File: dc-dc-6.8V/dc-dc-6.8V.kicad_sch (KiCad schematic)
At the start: 23 parts, among them P1 1.8mm_16AWG, P2 1.8mm_16AWG, P3 1.8mm_16AWG, P4 1.8mm_16AWG, Q3 DOD4185, U2 LM25085MY/NOPB

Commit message: update
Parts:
- removed C10: 1nF, bio-robot:C_0603_1608Metric, symbol bio-robot:C_1nF
- removed C11: 3.3nF, bio-robot:C_0603_1608Metric, symbol bio-robot:C_3.3nF
- removed C12: 47uF, bio-robot:CAP_EEEFT1H470AP, symbol bio-robot:Cpol_EEEFT1H470AP
- removed C9: 0.47u, bio-robot:C_0603_1608Metric, symbol bio-robot:C_0.47u
- removed D2: STPS20M100SG-TR, bio-robot:TO-263-2, symbol bio-robot:D_STPS20M100SG-TR
- removed L2: 3.3uH, bio-robot:IND_MDA1050-3R3M, symbol bio-robot:L_MDA1050-3R3M
- removed Q3: DOD4185, bio-robot:DPAK-3_ONS, symbol bio-robot:Q_Pch40V45A
- removed R3: 113k, bio-robot:R_0603_1608Metric, symbol bio-robot:R_113k
- removed R4: 4.12k, bio-robot:R_0603_1608Metric, symbol bio-robot:R_4.12k
- removed R5: 10m, bio-robot:R_0805_2012Metric, symbol bio-robot:R_10m_0805
- removed R8: 10k, bio-robot:R_0603_1608Metric, symbol bio-robot:R_10k
- removed R9: 2.26k, bio-robot:R_0603_1608Metric, symbol bio-robot:R_2.26k
- removed U2: LM25085MY/NOPB, bio-robot:MSOP8_PowerPad, symbol bio-robot:LM25085MY_NOPB
- added C3: 22u_1206, bots:C_1206_3216Metric, symbol bots:C_22u_1206
- added C4: 0.1u, bots:C_0603_1608Metric, symbol bots:C_0.1u
- added C5: 15nF, bio-robot:C_0603_1608Metric, symbol bio-robot:C_15nF
- added C6: 0.47u, bio-robot:C_0603_1608Metric, symbol bio-robot:C_0.47u
- added C7: 2.2u, bio-robot:C_0603_1608Metric, symbol bio-robot:C_2.2u
- added C8: 180pF, bio-robot:C_0603_1608Metric, symbol bio-robot:C_180pF
- added C9: 82uF, bio-robot:CAP_10SVPC120MV, symbol bio-robot:Cpol_82uF
- added L1: 1.8uH, bio-robot:IND_XAL7070_COC, symbol bio-robot:L_XAL7070-182MEC
- added Q1, Q2: SVD5865NLT4G, bots:DPAK-3_ONS, symbol bio-robot:Q_Nch60V46A
- added R1: 137k, bio-robot:R_0603_1608Metric, symbol bio-robot:R_137k
- added R2: 806R, bots:R_0603_1608Metric, symbol bio-robot:R_806R
- added R3: 9.76k, bots:R_0603_1608Metric, symbol bio-robot:R_9.76k
- added R4: 102k, bots:R_0603_1608Metric, symbol bio-robot:R_102k
- added U1: LM3150MHX_NOPB, bio-robot:SOP65P640X110-15N, symbol bio-robot:LM3150MHX_NOPB
- H1: renamed from H5; footprint MountingHole:MountingHole_3.2mm_M3_DIN965_Pad -> bio-robot:MountingHole_3.2mm_M3_DIN965_Pad
- H2: renamed from H6; footprint MountingHole:MountingHole_3.2mm_M3_DIN965_Pad -> bio-robot:MountingHole_3.2mm_M3_DIN965_Pad
- H3: renamed from H7; footprint MountingHole:MountingHole_3.2mm_M3_DIN965_Pad -> bio-robot:MountingHole_3.2mm_M3_DIN965_Pad
- H4: renamed from H8; footprint MountingHole:MountingHole_3.2mm_M3_DIN965_Pad -> bio-robot:MountingHole_3.2mm_M3_DIN965_Pad
- renumbered C8 to C1, C7 to C2
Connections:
- net +6.8V: now also C8.1, C9.1, L1.1, R4.1
- net CVCC: now also C7.1, U1.1 (VCC)
- net GND: now also C3.2, C4.2, C5.2, C7.2, C9.2, Q2.3 (S), R3.2, U1.14 (PGND), U1.15 (EXP), U1.5 (SGND_5), U1.9 (SGND_9)
- net VCC: now also C3.1, C4.1, Q1.2 (D), R1.1, U1.2 (VIN)
- new net BST: C6.1, U1.12 (BST)
- new net FB: C8.2, R3.1, R4.2, U1.4 (FB)
- new net HG: Q1.1 (G), U1.11 (HG)
- new net ILIM: R2.1, U1.8 (ILIM)
- new net LG: Q2.1 (G), U1.13 (LG)
- new net RON: R1.2, U1.7 (RON)
- new net SS: C5.1, U1.6 (SS)
- new net SW: C6.2, L1.2, Q1.3 (S), Q2.2 (D), R2.2, U1.10 (SW)
- no-connect marks 0 -> 1
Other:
- moved on the sheet: C1, C2, H1, H2, H3, H4, P1, P2, P3, P4

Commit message: update
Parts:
- removed Q1, Q2: SVD5865NLT4G, bots:DPAK-3_ONS, symbol bio-robot:Q_Nch60V46A
- added Q1, Q2: SVD5865NLT4G, bio-robot:SOIC-8_3.9x4.9mm_P1.27mm, symbol bio-robot:Q_Nch60V46A_SOIC8
- C1, C2, C3: footprint bots:C_1206_3216Metric -> bio-robot:C_1206_3216Metric; symbol bots:C_22u_1206 -> bio-robot:C_22u_1206
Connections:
- net GND: now also Q2.1 (S), Q2.2 (S), Q2.3 (S)
- net HG: now also Q1.4 (G)
- net LG: now also Q2.4 (G)
- net SW: now also Q1.1 (S), Q1.2 (S), Q1.3 (S), Q2.5 (D), Q2.6 (D), Q2.7 (D), Q2.8 (D)
- net VCC: now also Q1.5 (D), Q1.6 (D), Q1.7 (D), Q1.8 (D)

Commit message: update to silkscreen
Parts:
- Q1, Q2: value SVD5865NLT4G -> AO4354
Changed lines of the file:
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@@
 			)
 		)
-		(property "Value" "SVD5865NLT4G"
+		(property "Value" "AO4354"
 			(at 179.07 100.9649 0)
 			(show_name no)
@@
 			)
 		)
-		(property "Value" "SVD5865NLT4G"
+		(property "Value" "AO4354"
 			(at 179.07 67.9449 0)
 			(show_name no)

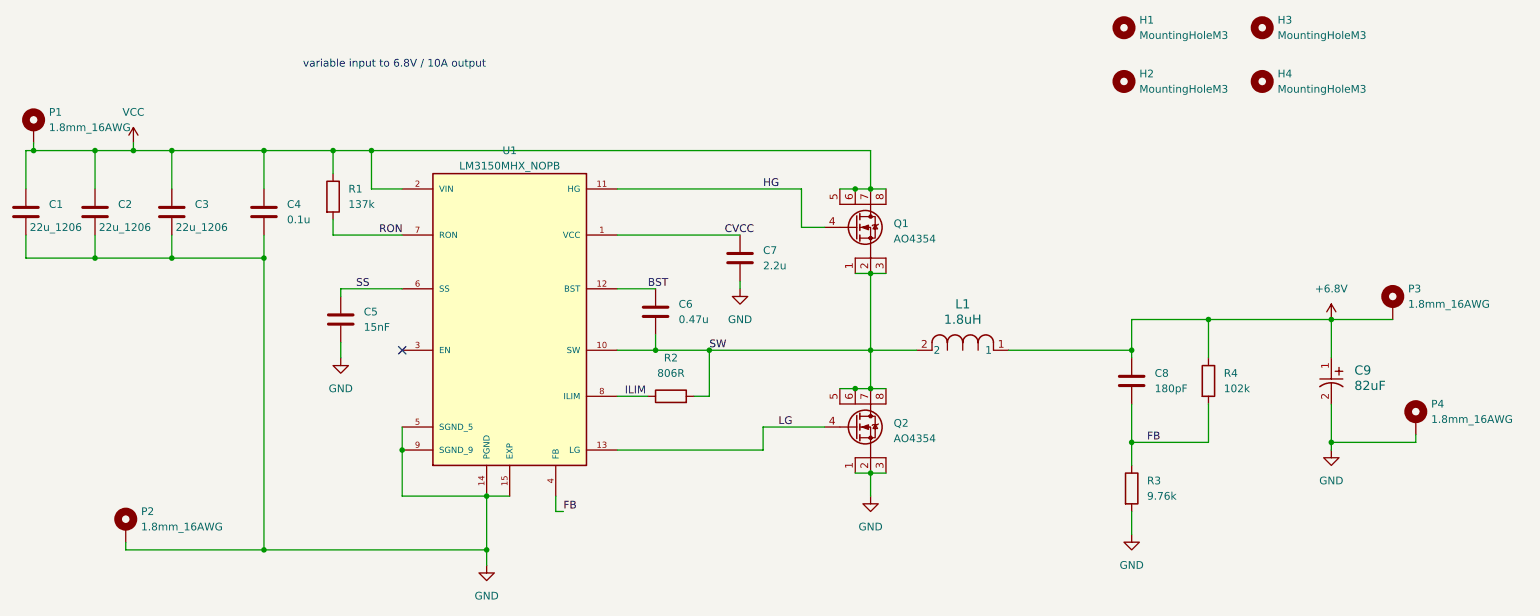
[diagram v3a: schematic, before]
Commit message: 5V 5A version
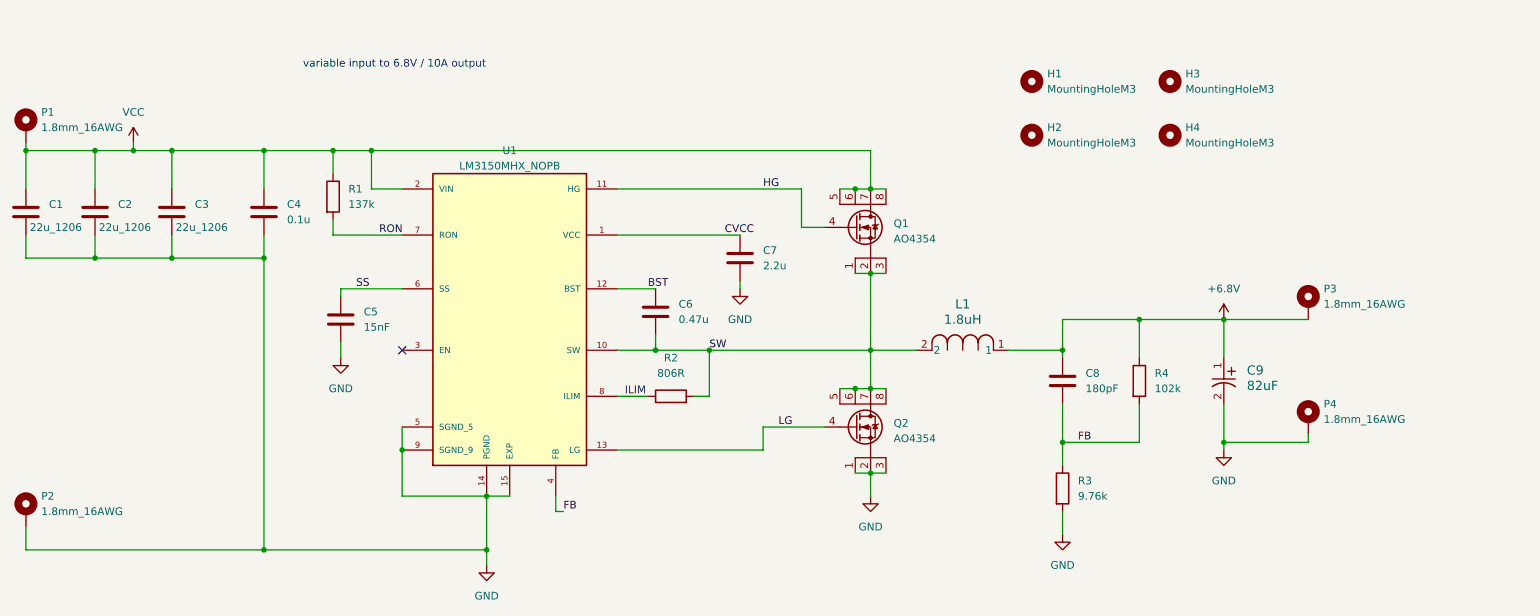
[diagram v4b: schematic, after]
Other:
- moved on the sheet: C8, C9, H1, H2, H3, H4, P1, P2, P3, P4, R3, R4

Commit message: ordered
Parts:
- removed R3: 9.76k, bots:R_0603_1608Metric, symbol bio-robot:R_9.76k
- removed R4: 102k, bots:R_0603_1608Metric, symbol bio-robot:R_102k
- added R3: 10k, bio-robot:R_0603_1608Metric, symbol bio-robot:R_10k
- added R4: 100k, bots:R_0603_1608Metric, symbol bio-robot:R_100k
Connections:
- net +6.8V: now also R4.1
- net FB: now also R3.1, R4.2
- net GND: now also R3.2

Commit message: naming
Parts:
- C9: value 82uF -> 120uF; symbol bio-robot:Cpol_82uF -> bio-robot:Cpol_120uF
- R4: value 100k -> 102k; footprint bots:R_0603_1608Metric -> bio-robot:R_0603_1608Metric; symbol bio-robot:R_100k -> bio-robot:R_102k; JLC Extended no -> yes; LCSC C25803 -> C203230; MPN 0603WAF1003T5E -> CR0603-FX-1023ELF; Manufacturer UNI-ROYAL(Uniroyal Elec) -> Bourns
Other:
- note added: "Synchronous Converter: Higher efficiency for large currents"
- moved on the sheet: C1, C2, C3, C4, C5, C7, C8, C9, H1, H2, H3, H4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
